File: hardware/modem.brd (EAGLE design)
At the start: 122.3 x 64.5 mm, 40 parts, among them IC1 MAX3238ECDB, IC2 74LS04D, IC4 LD117ADT33TR, U1 ESP-12S

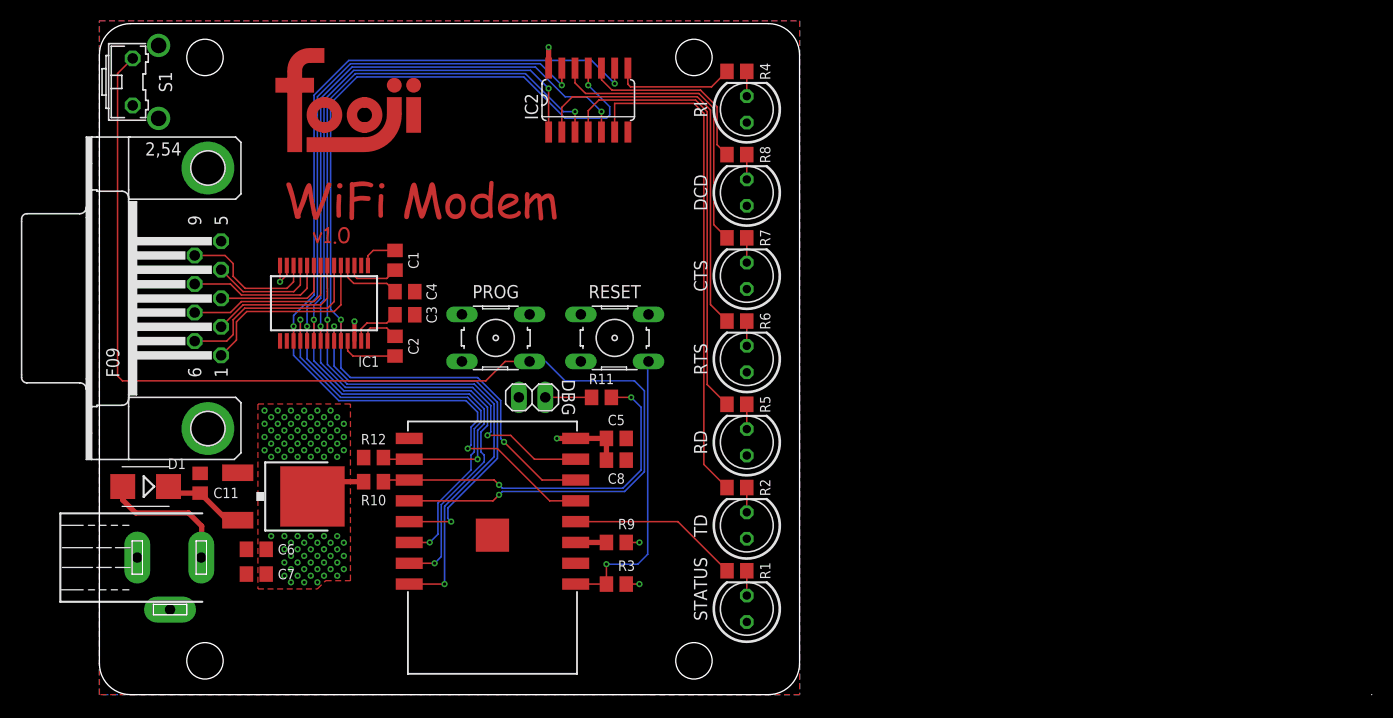
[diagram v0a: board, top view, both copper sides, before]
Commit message: fixed lots of minor problems of the first prototype
 - mount holes too large (3.2mm instead of 3.0mm)
 - missing keep-out around mount holes
 - resistor collides with screw in mount hole
 - button S1 collides with screw in mount hole
 - C6 and C7 were hard to solder, thermals on around caps
 - LEDs were hard to solder, thermals on VCC layer
 - debug port position and layout
 - cosmetic changes
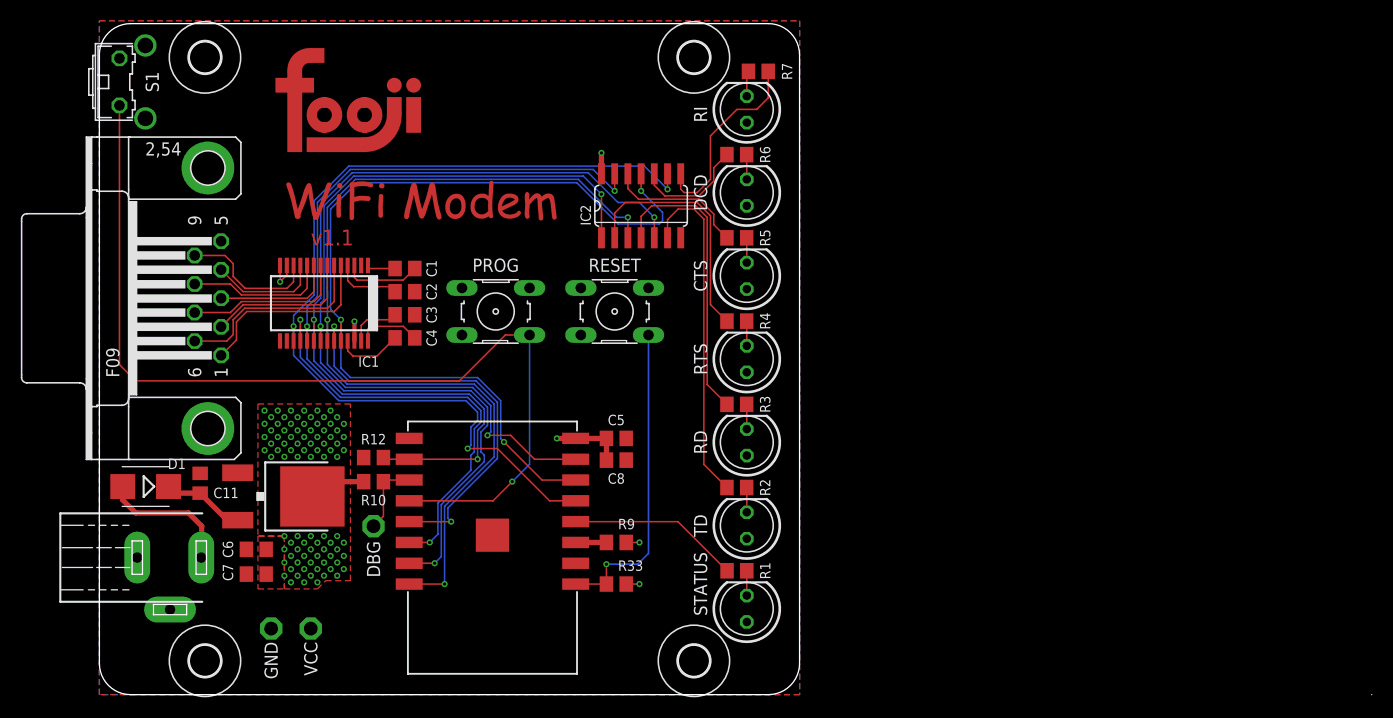
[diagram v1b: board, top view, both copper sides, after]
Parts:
- removed R11, R8: (no value), rcl:R0805
- added GND, VCC: PTR1PAD1-13, testpad:P1-13
- added H1, H2, H3, H4: MOUNT-HOLE3.0, holes:3,0
- added R33: 10k, rcl:R0805
- C1, C2, C3, C4: value 0.1µF -> 100n
- C7: value 10µF -> 100nF
- DBG: value (none) -> PTR1PAD1-13; device pinhead:1X02 -> testpad:P1-13
- R1, R2, R3, R4, R5, R6, R7: value (none) -> 820
- R10, R12, R9: value (none) -> 10k
- moved R4 24.0 mm to (61.3, 35.9)
- moved R3 20.8 mm to (61.3, 27.9)
- moved DBG 19.6 mm to (26.4, 16.2)
- moved R7 16.1 mm to (63.3, 59.9), turned to 180 degrees
- moved R5 16.0 mm to (61.3, 43.9)
- moved R6 16.0 mm to (61.3, 51.9)
- moved IC2 11.4 mm to (52.1, 47.0)
- moved C2 5.32 mm to (29.4, 38.7), turned to 0 degrees
- moved C4 4.45 mm to (29.4, 34.3), turned to 180 degrees
- moved PROG 2.54 mm to (38.1, 36.8)
- moved RESET 2.54 mm to (49.5, 36.8)
- moved S1 1.27 mm to (3.17, 58.9)
- moved C1 1.24 mm to (29.4, 41.0), turned to 0 degrees
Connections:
- removed net N$24: DBG.1, R11.2
- net !RESET: now also R33.1; no longer R3.1
- net +3V3: now also R33.2, VCC.TP; no longer R3.2
- net DEBUG: now also DBG.TP; no longer R11.1
- net GND: now also C2.2, GND.TP, S1.1; no longer C4.2, DBG.2, S1.2
- net N$10: now also R5.2; no longer R7.2
- net N$11: now also C2.1; no longer C4.1
- net N$15: now also C4.2; no longer C2.2
- net N$16: now also C4.1; no longer C2.1
- net N$17: now also R6.2; no longer R8.2
- net N$18: now also R7.2; no longer R4.2
- net N$19: now also R7.1; no longer R4.1
- net N$20: now also R6.1; no longer R8.1
- net N$21: now also R4.2; no longer R6.2
- net N$23: now also S1.2; no longer S1.1
- net N$6: now also R3.2; no longer R5.2
- net N$7: now also R3.1; no longer R5.1
- net N$8: now also R4.1; no longer R6.1
- net N$9: now also R5.1; no longer R7.1
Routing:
- net DEBUG: track 35.3 -> 7.31 mm, vias 2 -> 0
- net N$23: track 113.9 -> 92.3 mm
- net N$2: track 48.6 -> 32.8 mm
- net N$8: track 38.6 -> 23.3 mm
- net N$7: track 43.3 -> 28.1 mm
- net N$9: track 28.7 -> 13.5 mm
- net N$20: track 18.3 -> 10.9 mm
- net N$19: track 11.8 -> 18.8 mm
- net DCE_RTS: track 84.9 -> 79.9 mm
- net DCE_RI: track 96.2 -> 91.1 mm
- net DCE_DCD: track 92.1 -> 87.0 mm
- net DCE_RXD: track 96.0 -> 90.9 mm
- net DCE_TXD: track 97.8 -> 92.8 mm
- net DCE_CTS: track 87.6 -> 82.6 mm
- net N$24: track 4.45 -> 0.00 mm
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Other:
- board text added: "v1.1"
